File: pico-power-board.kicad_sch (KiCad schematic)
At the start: 74 parts, among them J1 Conn_02x10_Counter_Clockwise, J10 Conn_01x06_Male, J2 Conn_02x10_Counter_Clockwise, J3 Conn_02x10_Counter_Clockwise, J4 DC-053D-25A, J5 Conn_02x10_Counter_Clockwise, J6 Conn_02x10_Counter_Clockwise, J7 Conn_02x10_Counter_Clockwise, J8 Conn_01x20_Female, J9 Conn_01x20_Female, U1 INA219AxD, U3 TMP102AIDRLR, U4 K7803-500R3

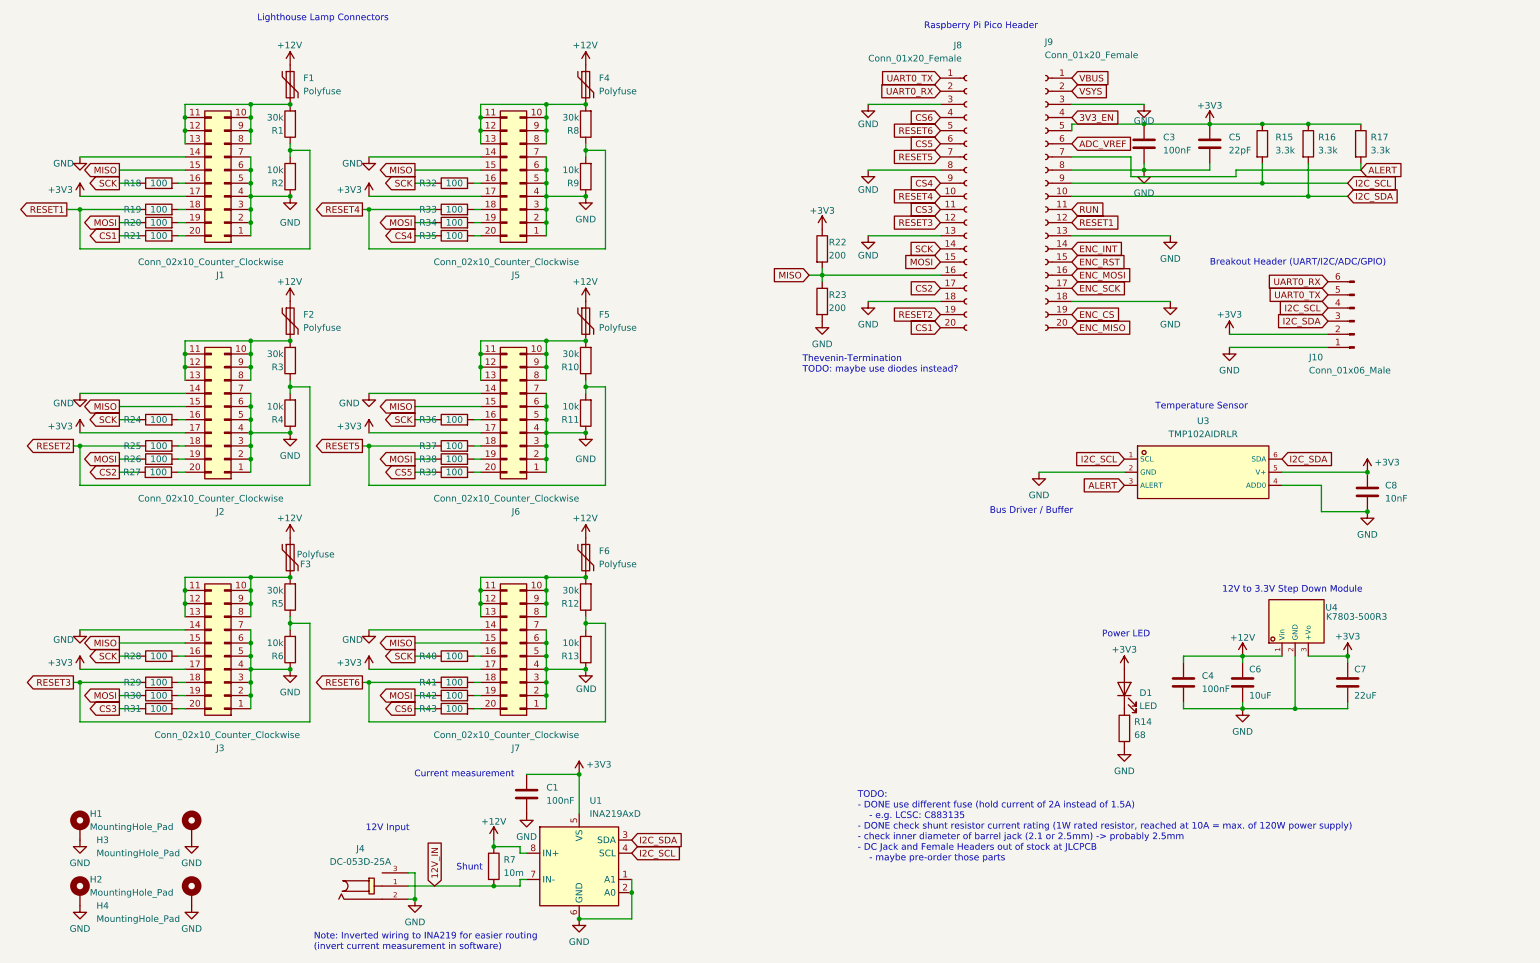
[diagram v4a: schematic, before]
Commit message: Refactor schematic and change temperature sensor from TMP102 to TMP112
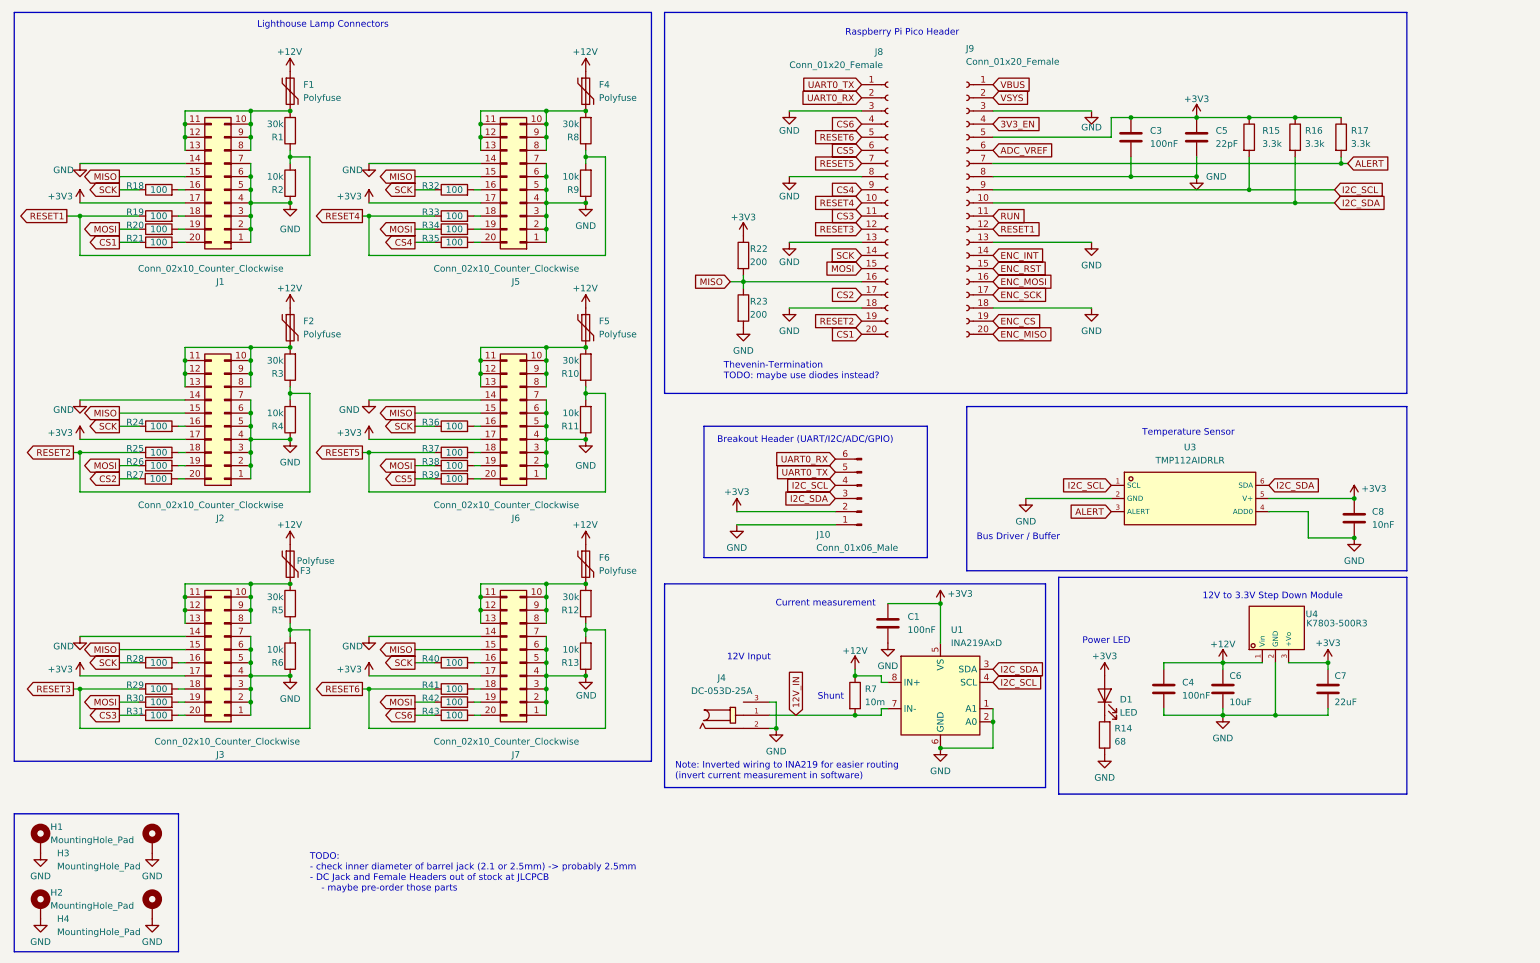
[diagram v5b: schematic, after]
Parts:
- U3: value TMP102AIDRLR -> TMP112AIDRLR; LCSC C99269 -> C28927
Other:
- note added: "TODO: - check inner diameter of barrel jack (2.1 or 2.5mm) -> probably 2.5mm - DC Jack and Female Headers out of stock at JLCPCB - maybe pre-order those parts"
- note removed: "TODO: - DONE use different fuse (hold current of 2A instead of 1.5A) - e.g. LCSC: C883135 - DONE check shunt resistor current rating (1W rated resistor, reached at 10A = max. of 120W power supply) - check inner diameter of barrel jack (2.1 or 2.5mm) -> probably 2.5mm - DC Jack and Female Headers out of stock at JLCPCB - maybe pre-order those parts"
- moved on the sheet: C1, C3, C4, C5, C6, C7, C8, D1, F1, F2, F3, F4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

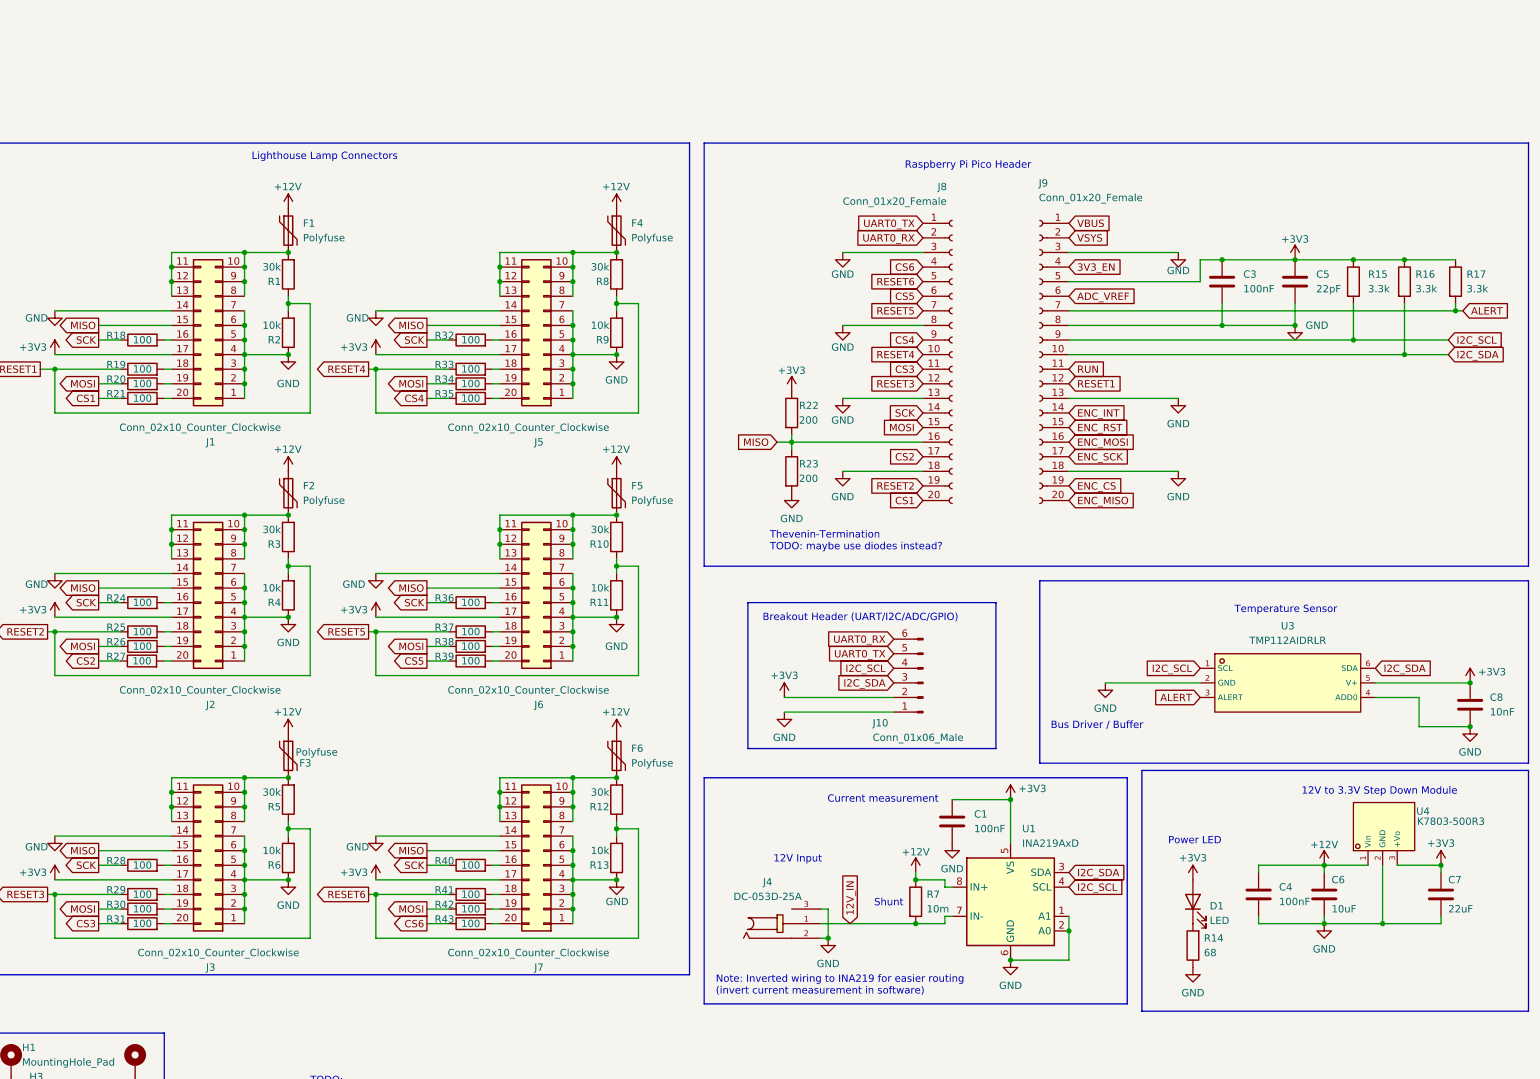
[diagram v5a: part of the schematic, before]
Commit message: Change DC-Jack to an available option, add logos and some trace refactoring
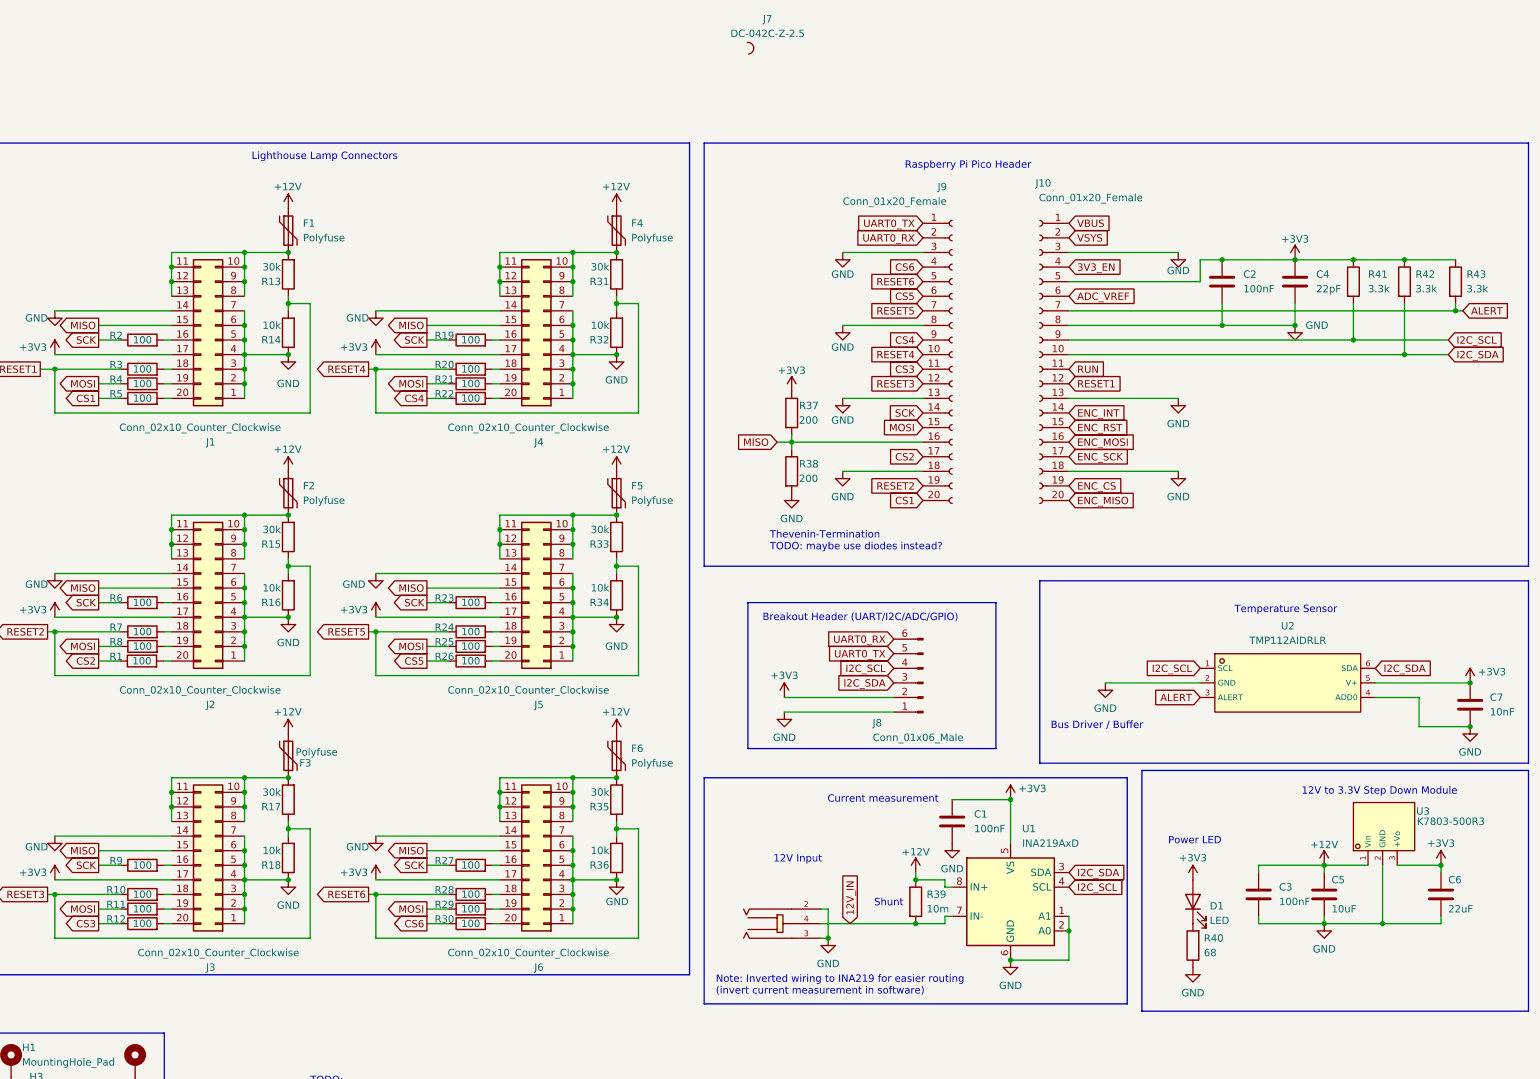
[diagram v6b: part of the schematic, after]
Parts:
- J7: renamed from J4; value DC-053D-25A -> DC-042C-Z-2.5; footprint Lighthouse:DC-IN-TH_DC-053D-25A-1 -> Lighthouse:DC-IN-TH_DC-042C-Z-2.5; symbol DC-Jack:DC-053D-25A -> DC-Jack-XKBConnectivity:DC-042C-Z-2_5; LCSC C2686352 -> C2880557
- R1: renamed from R27; JLC (none) -> 0603; LCSC (none) -> C881354
- R10: renamed from R29; JLC (none) -> 0603; LCSC (none) -> C881354
- R11: renamed from R30; JLC (none) -> 0603; LCSC (none) -> C881354
- R12: renamed from R31; JLC (none) -> 0603; LCSC (none) -> C881354
- R19: renamed from R32; JLC (none) -> 0603; LCSC (none) -> C881354
- R2: renamed from R18; JLC (none) -> 0603; LCSC (none) -> C881354
- R20: renamed from R33; JLC (none) -> 0603; LCSC (none) -> C881354
- R21: renamed from R34; JLC (none) -> 0603; LCSC (none) -> C881354
- R22: renamed from R35; JLC (none) -> 0603; LCSC (none) -> C881354
- R23: renamed from R36; JLC (none) -> 0603; LCSC (none) -> C881354
- R24: renamed from R37; JLC (none) -> 0603; LCSC (none) -> C881354
- R25: renamed from R38; JLC (none) -> 0603; LCSC (none) -> C881354
- R26: renamed from R39; JLC (none) -> 0603; LCSC (none) -> C881354
- R27: renamed from R40; JLC (none) -> 0603; LCSC (none) -> C881354
- R28: renamed from R41; JLC (none) -> 0603; LCSC (none) -> C881354
- R29: renamed from R42; JLC (none) -> 0603; LCSC (none) -> C881354
- R3: renamed from R19; JLC (none) -> 0603; LCSC (none) -> C881354
- R30: renamed from R43; JLC (none) -> 0603; LCSC (none) -> C881354
- R37: renamed from R22; footprint Resistor_SMD:R_0603_1608Metric -> Resistor_SMD:R_0805_2012Metric; JLC (none) -> 0805; LCSC (none) -> C881261
- R38: renamed from R23; footprint Resistor_SMD:R_0603_1608Metric -> Resistor_SMD:R_0805_2012Metric; JLC (none) -> 0805; LCSC (none) -> C881261
- R4: renamed from R20; JLC (none) -> 0603; LCSC (none) -> C881354
- R5: renamed from R21; JLC (none) -> 0603; LCSC (none) -> C881354
- R6: renamed from R24; JLC (none) -> 0603; LCSC (none) -> C881354
- R7: renamed from R25; JLC (none) -> 0603; LCSC (none) -> C881354
- R8: renamed from R26; JLC (none) -> 0603; LCSC (none) -> C881354
- R9: renamed from R28; JLC (none) -> 0603; LCSC (none) -> C881354
- U3: renamed from U4; LCSC C86736 -> C909766
- renumbered C3 to C2, C4 to C3, C5 to C4, C6 to C5, C7 to C6, C8 to C7, J9 to J10, J5 to J4, J6 to J5, J7 to J6, J10 to J8, J8 to J9, R1 to R13, R2 to R14, R3 to R15, R4 to R16, R5 to R17, R6 to R18, R8 to R31, R9 to R32, R10 to R33, R11 to R34, R12 to R35, R13 to R36, R7 to R39, R14 to R40, R15 to R41, R16 to R42, R17 to R43, U3 to U2
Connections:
- net 12V_IN: now also J7.4; no longer J7.1

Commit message: Add tri-state buffers to each connectors MISO line in order to Thevenin-terminate them separately and add decoupling capacitors to the termination, change LED and series resistor, change I2C pull-ups, add CS pull-ups, add MISO pull-down (after buffers)
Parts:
- removed R37, R38: 200, Resistor_SMD:R_0805_2012Metric, symbol Device:R
- added C10, C11, C12, C13, C8, C9: 100nF, Capacitor_SMD:C_0603_1608Metric, symbol Device:C
- added R42, R43, R44, R45, R46, R47, R48, R49, R50, R51, R52, R53: 200, Resistor_SMD:R_0603_1608Metric, symbol Device:R
- added R54, R55, R56, R57, R58, R59: 100, Resistor_SMD:R_0603_1608Metric, symbol Device:R
- added R60, R61, R62, R63, R64, R65, R66: 10k, Resistor_SMD:R_0603_1608Metric, symbol Device:R
- added U4, U5, U6, U7, U8, U9: 74LVC1G125GW,125, Lighthouse:SOT-353_L2.1-W1.3-P0.65-LS2.3-BR, symbol 74LVC1G125GW,125:74LVC1G125GW,125
- D1: LCSC C72038 -> C5151481
- R38: renamed from R40; value 68 -> 470; footprint Resistor_SMD:R_0603_1608Metric -> Resistor_SMD:R_0805_2012Metric; JLC 0603 -> 0805; LCSC C27592 -> C3152234
- R39: renamed from R41; value 3.3k -> 4.7k; LCSC C22978 -> C88615
- R40: renamed from R42; value 3.3k -> 4.7k; LCSC C22978 -> C88615
- R41: renamed from R43; value 3.3k -> 4.7k; LCSC C22978 -> C88615
- renumbered C7 to C1, C1 to C2, C2 to C4, C4 to C6, C6 to C7, R39 to R37, U2 to U1, U1 to U2
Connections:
- net +3V3: now also C10.1, C11.1, C12.1, C13.1, C8.1, C9.1, R42.1, R44.1, R46.1, R48.1, R50.1, R52.1, R60.1, R61.1, R62.1, R63.1, R64.1, R65.1, U4.5 (VCC), U5.5 (VCC), U6.5 (VCC), U7.5 (VCC), U8.5 (VCC), U9.5 (VCC)
- net CS1: now also R60.2, U4.1 (1OE#)
- net CS2: now also R61.2, U5.1 (1OE#)
- net CS3: now also R62.2, U6.1 (1OE#)
- net CS4: now also R63.2, U7.1 (1OE#)
- net CS5: now also R64.2, U8.1 (1OE#)
- net CS6: now also R65.2, U9.1 (1OE#)
- net GND: now also C10.2, C11.2, C12.2, C13.2, C8.2, C9.2, R43.2, R45.2, R47.2, R49.2, R51.2, R53.2, R66.2, U4.3 (GND), U5.3 (GND), U6.3 (GND), U7.3 (GND), U8.3 (GND), U9.3 (GND)
- net MISO: now also R54.2, R55.2, R56.2, R57.2, R58.2, R59.2, R66.1; no longer J1.15 (Pin_15), J2.15 (Pin_15), J3.15 (Pin_15), J4.15 (Pin_15), J5.15 (Pin_15), J6.15 (Pin_15)
- new net: R56.1, U6.4 (Y)
- new net: R55.1, U5.4 (Y)
- new net: R58.1, U8.4 (Y)
- new net: R57.1, U7.4 (Y)
- new net: R54.1, U4.4 (Y)
- new net: R59.1, U9.4 (Y)
- new net MISO_1: J1.15 (Pin_15), R42.2, R43.1, U4.2 (A)
- new net MISO_2: J2.15 (Pin_15), R44.2, R45.1, U5.2 (A)
- new net MISO_3: J3.15 (Pin_15), R46.2, R47.1, U6.2 (A)
- new net MISO_4: J4.15 (Pin_15), R48.2, R49.1, U7.2 (A)
- new net MISO_5: J5.15 (Pin_15), R50.2, R51.1, U8.2 (A)
- new net MISO_6: J6.15 (Pin_15), R52.2, R53.1, U9.2 (A)
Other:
- note added: "Separate Thevenin termination for each connectors MISO line Tri-State buffer enables MISO line with CS -> demultiplexing"
- note added: "TODO: - does voltage divider on reset line or pull ups on chip-select affect termination and voltage level? - check inner diameter of barrel jack (2.1 or 2.5mm) -> probably 2.5mm - DC Jack and Female Headers often out of stock at JLCPCB - maybe pre-order those parts"
- note removed: "Bus Driver / Buffer"
- note removed: "TODO: - check inner diameter of barrel jack (2.1 or 2.5mm) -> probably 2.5mm - DC Jack and Female Headers out of stock at JLCPCB - maybe pre-order those parts"
- note removed: "Thevenin-Termination TODO: maybe use diodes instead?"
- moved on the sheet: C1, C2, C3, C4, C5, C6, C7, D1, F1, F2, F3, F4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
